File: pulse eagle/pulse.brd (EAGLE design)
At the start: 21 x 31.1 mm, 24 parts, among them IC1 LM358D, J1 ISP Touch, T1 BC846, Y1 8MHz

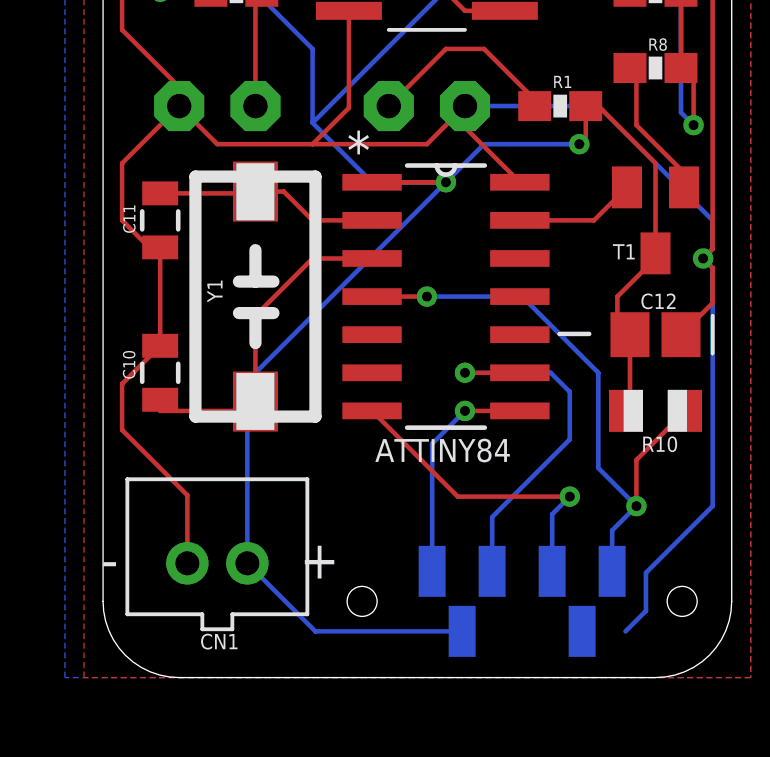
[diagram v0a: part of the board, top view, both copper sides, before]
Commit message: Adding serial port headers.
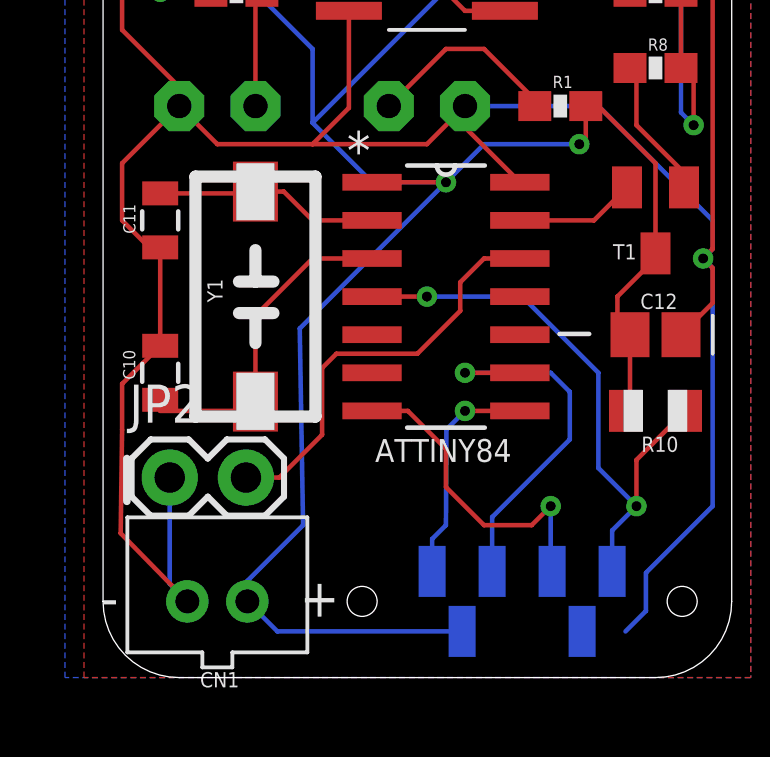
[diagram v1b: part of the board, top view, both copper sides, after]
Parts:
- added JP2: M02PTH, SparkFun-Connectors:1X02
- moved CN1 1.27 mm to (3.81, 2.54)
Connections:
- new net SERIAL: ATTINY84.12, JP2.2
- net GND: now also JP2.1
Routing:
- net SERIAL: track 0.00 -> 14.0 mm
- net GND: track 100.4 -> 106.1 mm
- net VCC: track 75.3 -> 76.1 mm
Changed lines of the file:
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@@
 <wire x1="9.525" y1="21.59" x2="12.065" y2="21.59" width="0.127" layer="21"/>
 <wire x1="11.1125" y1="26.67" x2="10.4775" y2="26.67" width="0.127" layer="21" curve="-180"/>
+<wire x1="0.79375" y1="7.3025" x2="0.79375" y2="5.87375" width="0.254" layer="21"/>
 </plain>
 <attributes>
@@
 <attribute name="VALUE" x="9.30275" y="5.55625" size="1.016" layer="28" rot="MR180"/>
 </element>
-<element name="CN1" library="adafruit" package="JST-PH-2-THM" value="" x="3.81" y="3.81" smashed="yes">
-<attribute name="NAME" x="3.2325" y="0.945" size="0.508" layer="25" font="vector"/>
+<element name="CN1" library="adafruit" package="JST-PH-2-THM" value="" x="3.81" y="2.54" smashed="yes">
+<attribute name="NAME" x="3.2325" y="-0.325" size="0.508" layer="25" font="vector"/>
 </element>
 <element name="R1" library="SparkFun-Resistors" package="0603-RES" value="220" x="15.24" y="19.05" smashed="yes">
@@
 <attribute name="VALUE" x="0.6096" y="17.2466" size="1.27" layer="28" ratio="10" rot="MR0"/>
 </element>
+<element name="JP2" library="SparkFun-Connectors" package="1X02" value="M02PTH" x="2.2225" y="6.6675"/>
 </elements>
 <signals>
@@
 <wire x1="12.065" y1="19.05" x2="12.065" y2="18.3388" width="0.1524" layer="1"/>
 <wire x1="12.065" y1="18.3388" x2="13.8938" y2="16.51" width="0.1524" layer="1"/>
-<wire x1="2.81" y1="3.81" x2="2.81" y2="6.08" width="0.1524" layer="1"/>
-<wire x1="2.81" y1="6.08" x2="0.635" y2="8.255" width="0.1524" layer="1"/>
+<wire x1="2.81" y1="2.54" x2="0.5875" y2="4.81" width="0.1524" layer="1"/>
+<wire x1="0.5875" y1="4.81" x2="0.635" y2="8.255" width="0.1524" layer="1"/>
 <wire x1="0.635" y1="8.255" x2="0.635" y2="9.79" width="0.1524" layer="1"/>
 <wire x1="0.635" y1="9.79" x2="1.905" y2="11.06" width="0.1524" layer="1"/>
@@
 <wire x1="8.195" y1="18.99" x2="6.985" y2="17.78" width="0.1524" layer="1"/>
 <contactref element="J1" pad="6"/>
+<contactref element="JP2" pad="1"/>
+<wire x1="2.2225" y1="6.6675" x2="2.2225" y2="3.1275" width="0.1524" layer="16"/>
+<wire x1="2.2225" y1="3.1275" x2="2.81" y2="2.54" width="0.1524" layer="16"/>
 </signal>
 <signal name="MISO">
 <contactref element="ATTINY84" pad="8"/>
 <contactref element="J1" pad="1"/>
-<wire x1="10.97" y1="3.54" x2="10.97" y2="7.795" width="0.1524" layer="16"/>
-<wire x1="10.97" y1="7.795" x2="12.065" y2="8.89" width="0.1524" layer="16"/>
+<wire x1="10.97" y1="3.54" x2="10.97" y2="4.62" width="0.1524" layer="16"/>
+<wire x1="10.97" y1="4.62" x2="11.43" y2="5.08" width="0.1524" layer="16"/>
+<wire x1="11.43" y1="5.08" x2="11.44625" y2="8.27125" width="0.1524" layer="16"/>
+<wire x1="11.44625" y1="8.27125" x2="12.065" y2="8.89" width="0.1524" layer="16"/>
 <via x="12.065" y="8.89" extent="1-16" drill="0.3302"/>
 <wire x1="12.065" y1="8.89" x2="13.8938" y2="8.89" width="0.1524" layer="1"/>
@@
 <contactref element="ATTINY84" pad="7"/>
 <contactref element="J1" pad="4"/>
-<wire x1="14.97" y1="3.54" x2="14.97" y2="5.445" width="0.1524" layer="16"/>
-<wire x1="14.97" y1="5.445" x2="15.5575" y2="6.0325" width="0.1524" layer="16"/>
-<via x="15.5575" y="6.0325" extent="1-16" drill="0.3302"/>
-<wire x1="15.5575" y1="6.0325" x2="11.8237" y2="6.0325" width="0.1524" layer="1"/>
-<wire x1="11.8237" y1="6.0325" x2="8.9662" y2="8.89" width="0.1524" layer="1"/>
+<wire x1="8.9662" y1="8.89" x2="10.16" y2="8.89" width="0.1524" layer="1"/>
+<wire x1="10.16" y1="8.89" x2="11.43" y2="7.62" width="0.1524" layer="1"/>
+<wire x1="11.43" y1="7.62" x2="11.43" y2="6.35" width="0.1524" layer="1"/>
+<wire x1="11.43" y1="6.35" x2="12.7" y2="5.08" width="0.1524" layer="1"/>
+<wire x1="12.7" y1="5.08" x2="14.2875" y2="5.08" width="0.1524" layer="1"/>
+<wire x1="14.2875" y1="5.08" x2="14.9225" y2="5.715" width="0.1524" layer="1"/>
+<via x="14.9225" y="5.715" extent="1-16" drill="0.3302"/>
+<wire x1="14.9225" y1="5.715" x2="14.9225" y2="3.5875" width="0.1524" layer="16"/>
+<wire x1="14.9225" y1="3.5875" x2="14.97" y2="3.54" width="0.1524" layer="16"/>
 </signal>
 <signal name="SCK">
@@
 <via x="11.43" y="16.51" extent="1-16" drill="0.3302"/>
 <wire x1="11.43" y1="16.51" x2="8.9662" y2="16.51" width="0.1524" layer="1"/>
-<wire x1="4.81" y1="3.81" x2="4.81" y2="9.89" width="0.1524" layer="16"/>
-<wire x1="4.81" y1="9.89" x2="11.43" y2="16.51" width="0.1524" layer="16"/>
+<wire x1="4.81" y1="2.54" x2="4.81" y2="3.2225" width="0.1524" layer="16"/>
+<wire x1="4.81" y1="3.2225" x2="6.6675" y2="5.08" width="0.1524" layer="16"/>
+<wire x1="6.6675" y1="5.08" x2="6.55625" y2="11.63625" width="0.1524" layer="16"/>
+<wire x1="6.55625" y1="11.63625" x2="11.43" y2="16.51" width="0.1524" layer="16"/>
 <wire x1="16.09" y1="19.05" x2="16.09" y2="17.995" width="0.1524" layer="1"/>
 <wire x1="16.09" y1="17.995" x2="15.875" y2="17.78" width="0.1524" layer="1"/>
@@
 <wire x1="15.875" y1="17.78" x2="12.7" y2="17.78" width="0.1524" layer="16"/>
 <wire x1="12.7" y1="17.78" x2="11.43" y2="16.51" width="0.1524" layer="16"/>
-<wire x1="11.97" y1="1.54" x2="7.08" y2="1.54" width="0.1524" layer="16"/>
-<wire x1="7.08" y1="1.54" x2="4.81" y2="3.81" width="0.1524" layer="16"/>
+<wire x1="11.97" y1="1.54" x2="5.81" y2="1.54" width="0.1524" layer="16"/>
+<wire x1="5.81" y1="1.54" x2="4.81" y2="2.54" width="0.1524" layer="16"/>
 <contactref element="IC1" pad="8"/>
 <wire x1="13.395" y1="26.035" x2="14.605" y2="26.035" width="0.1524" layer="1"/>
@@
 <wire x1="16.365" y1="15.24" x2="17.465" y2="16.34" width="0.1524" layer="1"/>
 </signal>
+<signal name="SERIAL">
+<contactref element="ATTINY84" pad="12"/>
+<contactref element="JP2" pad="2"/>
+<wire x1="4.7625" y1="6.6675" x2="5.87375" y2="6.6675" width="0.1524" layer="1"/>
+<wire x1="5.87375" y1="6.6675" x2="7.3025" y2="8.09625" width="0.1524" layer="1"/>
+<wire x1="7.3025" y1="8.09625" x2="7.3025" y2="10.31875" width="0.1524" layer="1"/>
+<wire x1="7.3025" y1="10.31875" x2="7.77875" y2="10.795" width="0.1524" layer="1"/>
+<wire x1="7.77875" y1="10.795" x2="10.4775" y2="10.795" width="0.1524" layer="1"/>
+<wire x1="10.4775" y1="10.795" x2="11.90625" y2="12.22375" width="0.1524" layer="1"/>
+<wire x1="11.90625" y1="12.22375" x2="11.90625" y2="13.17625" width="0.1524" layer="1"/>
+<wire x1="11.90625" y1="13.17625" x2="12.7" y2="13.97" width="0.1524" layer="1"/>
+<wire x1="12.7" y1="13.97" x2="13.8938" y2="13.97" width="0.1524" layer="1"/>
+</signal>
 </signals>

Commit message: Rev. A of the board.
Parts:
- C1, C3: value .1uf -> 1uf
- C12: value .1uf -> .1uF
- C2, C4: value 15pF -> .1uF
- R2: value 220 -> 39k
- R3, R5: value 220 -> 68k
- R4: value 220 -> 8.2k
- R6: value 220 -> 1k
- R7: value 220 -> 470k
- R8: value 220 -> 1.8k
- T1: value BC846 -> MMBT3904
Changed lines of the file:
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@@
 <attribute name="VALUE" x="7.9756" y="20.1168" size="2.0828" layer="27" ratio="10" rot="SR0"/>
 </element>
-<element name="C12" library="adafruit" package="C0805" value=".1uf" x="18.415" y="11.43" smashed="yes">
+<element name="C12" library="adafruit" package="C0805" value=".1uF" x="18.415" y="11.43" smashed="yes">
 <attribute name="NAME" x="19.14525" y="12.79525" size="0.508" layer="25" rot="R180"/>
 </element>
@@
 <attribute name="NAME" x="14.986" y="19.65325" size="0.4064" layer="25" font="vector"/>
 </element>
-<element name="R2" library="SparkFun-Resistors" package="0603-RES" value="220" x="4.445" y="22.86" smashed="yes" rot="R180">
+<element name="R2" library="SparkFun-Resistors" package="0603-RES" value="39k" x="4.445" y="22.86" smashed="yes" rot="R180">
 <attribute name="PROD_ID" value="RES-07866" x="-26.035" y="64.77" size="1.778" layer="27" rot="R180" display="off"/>
 <attribute name="NAME" x="6.00075" y="23.27275" size="0.4064" layer="25" font="vector" rot="R270"/>
 </element>
-<element name="R3" library="SparkFun-Resistors" package="0603-RES" value="220" x="3.175" y="27.94" smashed="yes" rot="R180">
+<element name="R3" library="SparkFun-Resistors" package="0603-RES" value="68k" x="3.175" y="27.94" smashed="yes" rot="R180">
 <attribute name="PROD_ID" value="RES-07866" x="-31.115" y="69.85" size="1.778" layer="27" rot="R180" display="off"/>
 <attribute name="NAME" x="4.73075" y="28.35275" size="0.4064" layer="25" font="vector" rot="R270"/>
 </element>
-<element name="R4" library="SparkFun-Resistors" package="0603-RES" value="220" x="6.985" y="29.21" smashed="yes">
+<element name="R4" library="SparkFun-Resistors" package="0603-RES" value="8.2k" x="6.985" y="29.21" smashed="yes">
 <attribute name="PROD_ID" value="RES-07866" x="45.085" y="-12.7" size="1.778" layer="27" display="off"/>
 <attribute name="NAME" x="6.731" y="29.81325" size="0.4064" layer="25" font="vector"/>
 </element>
-<element name="R5" library="SparkFun-Resistors" package="0603-RES" value="220" x="18.415" y="29.21" smashed="yes" rot="R180">
+<element name="R5" library="SparkFun-Resistors" package="0603-RES" value="68k" x="18.415" y="29.21" smashed="yes" rot="R180">
 <attribute name="PROD_ID" value="RES-07866" x="-23.495" y="71.12" size="1.778" layer="27" rot="R180" display="off"/>
 <attribute name="NAME" x="18.82775" y="30.19425" size="0.4064" layer="25" font="vector" rot="R180"/>
 </element>
-<element name="R6" library="SparkFun-Resistors" package="0603-RES" value="220" x="18.415" y="26.67" smashed="yes" rot="R180">
+<element name="R6" library="SparkFun-Resistors" package="0603-RES" value="1k" x="18.415" y="26.67" smashed="yes" rot="R180">
 <attribute name="PROD_ID" value="RES-07866" x="-27.305" y="68.58" size="1.778" layer="27" rot="R180" display="off"/>
 <attribute name="NAME" x="16.47825" y="27.08275" size="0.4064" layer="25" font="vector" rot="R270"/>
 </element>
-<element name="R7" library="SparkFun-Resistors" package="0603-RES" value="220" x="18.415" y="22.86" smashed="yes" rot="R180">
+<element name="R7" library="SparkFun-Resistors" package="0603-RES" value="470k" x="18.415" y="22.86" smashed="yes" rot="R180">
 <attribute name="PROD_ID" value="RES-07866" x="3.175" y="68.58" size="1.778" layer="27" rot="R180" display="off"/>
 <attribute name="NAME" x="16.47825" y="23.27275" size="0.4064" layer="25" font="vector" rot="R270"/>
 </element>
-<element name="R8" library="SparkFun-Resistors" package="0603-RES" value="220" x="18.415" y="20.32" smashed="yes">
+<element name="R8" library="SparkFun-Resistors" package="0603-RES" value="1.8k" x="18.415" y="20.32" smashed="yes">
 <attribute name="PROD_ID" value="RES-07866" x="37.465" y="-25.4" size="1.778" layer="27" display="off"/>
 <attribute name="NAME" x="18.82775" y="21.30425" size="0.4064" layer="25" font="vector" rot="R180"/>
 </element>
-<element name="C1" library="adafruit" package="C0805" value=".1uf" x="3.175" y="25.4" smashed="yes" rot="R180">
+<element name="C1" library="adafruit" package="C0805" value="1uf" x="3.175" y="25.4" smashed="yes" rot="R180">
 <attribute name="NAME" x="4.826" y="25.9715" size="0.508" layer="25" rot="R270"/>
 </element>
-<element name="C3" library="adafruit" package="C0805" value=".1uf" x="14.605" y="29.21" smashed="yes">
+<element name="C3" library="adafruit" package="C0805" value="1uf" x="14.605" y="29.21" smashed="yes">
 <attribute name="NAME" x="14.19225" y="30.226" size="0.508" layer="25"/>
 </element>
-<element name="C2" library="SparkFun-Passives" package="0805" value="15pF" x="10.795" y="29.21" smashed="yes">
+<element name="C2" library="SparkFun-Passives" package="0805" value=".1uF" x="10.795" y="29.21" smashed="yes">
 <attribute name="NAME" x="10.50925" y="30.0355" size="0.4064" layer="25"/>
 </element>
-<element name="C4" library="SparkFun-Passives" package="0805" value="15pF" x="18.415" y="24.765" smashed="yes">
+<element name="C4" library="SparkFun-Passives" package="0805" value=".1uF" x="18.415" y="24.765" smashed="yes">
 <attribute name="NAME" x="16.9545" y="24.47925" size="0.4064" layer="25" rot="R90"/>
 </element>
-<element name="T1" library="transistor" package="SOT23" value="BC846" x="18.415" y="15.24" smashed="yes" rot="R180">
+<element name="T1" library="transistor" package="SOT23" value="MMBT3904" x="18.415" y="15.24" smashed="yes" rot="R180">
 <attribute name="NAME" x="17.78" y="14.44625" size="0.508" layer="25" rot="R180"/>
 </element>

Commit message: Moving pins around.
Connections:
- net A0: now also ATTINY84.12; no longer ATTINY84.13
- net SERIAL: now also ATTINY84.11; no longer ATTINY84.12
- net VCC: now also ATTINY84.13
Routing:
- net A0: track 4.03 -> 1.56 mm
- net SERIAL: track 14.0 -> 12.8 mm
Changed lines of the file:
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@@
 <layer number="112" name="tSilk" color="7" fill="1" visible="yes" active="yes"/>
 <layer number="116" name="Patch_BOT" color="9" fill="4" visible="yes" active="yes"/>
+<layer number="118" name="Rect_Pads" color="7" fill="1" visible="no" active="no"/>
 <layer number="121" name="_tsilk" color="7" fill="1" visible="yes" active="yes"/>
 <layer number="122" name="_bsilk" color="7" fill="1" visible="yes" active="yes"/>
@@
 <wire x1="15.875" y1="27.305" x2="15.7988" y2="27.305" width="0.1524" layer="16"/>
 <wire x1="15.7988" y1="27.305" x2="6.985" y2="18.4912" width="0.1524" layer="16"/>
+<contactref element="ATTINY84" pad="13"/>
+<wire x1="11.43" y1="16.51" x2="13.8938" y2="15.24" width="0" layer="19" extent="1-16"/>
 </signal>
 <signal name="RESET">
@@
 </signal>
 <signal name="A0">
-<contactref element="ATTINY84" pad="13"/>
 <contactref element="T1" pad="2"/>
-<wire x1="13.8938" y1="15.24" x2="16.365" y2="15.24" width="0.1524" layer="1"/>
 <wire x1="16.365" y1="15.24" x2="17.465" y2="16.34" width="0.1524" layer="1"/>
+<contactref element="ATTINY84" pad="12"/>
+<wire x1="13.8938" y1="13.97" x2="16.365" y2="15.24" width="0" layer="19" extent="1-1"/>
 </signal>
 <signal name="SERIAL">
-<contactref element="ATTINY84" pad="12"/>
 <contactref element="JP2" pad="2"/>
 <wire x1="4.7625" y1="6.6675" x2="5.87375" y2="6.6675" width="0.1524" layer="1"/>
@@
 <wire x1="11.90625" y1="12.22375" x2="11.90625" y2="13.17625" width="0.1524" layer="1"/>
 <wire x1="11.90625" y1="13.17625" x2="12.7" y2="13.97" width="0.1524" layer="1"/>
-<wire x1="12.7" y1="13.97" x2="13.8938" y2="13.97" width="0.1524" layer="1"/>
+<contactref element="ATTINY84" pad="11"/>
+<wire x1="12.7" y1="13.97" x2="13.8938" y2="12.7" width="0" layer="19" extent="1-1"/>
 </signal>
 </signals>
